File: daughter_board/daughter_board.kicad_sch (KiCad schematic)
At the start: 30 parts, among them J1 Conn_01x05_Female, J3 Conn_01x06_Male, J4 Conn_01x06_Male, J5 Conn_01x02_Male, J6 Conn_01x02_Male, J7 Conn_01x06_Male, J8 Conn_01x06_Male, U1 ATmega32U4-A, U2 DRV8833PW, U3 DRV8833PW, U4 DRV8833PW, Y1 Crystal

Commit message: im so tired
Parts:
- removed C10: 0.1uF, Capacitor_SMD:C_0805_2012Metric, symbol Device:C_Small
- removed C12: 2.2uF, Capacitor_SMD:C_0805_2012Metric, symbol Device:C_Small
- removed C13: 10uF, Capacitor_SMD:C_0805_2012Metric, symbol Device:C_Small
- removed J5, J6: Conn_01x02_Male, Connector_PinHeader_1.27mm:PinHeader_1x02_P1.27mm_Vertical, symbol Connector:Conn_01x02_Male
- removed U3: DRV8833PW, Package_SO:TSSOP-16_4.4x5mm_P0.65mm, symbol Driver_Motor:DRV8833PW
- added SW1: SW_Push, Button_Switch_SMD:SW_SPST_EVPBF, symbol Switch:SW_Push
- C1, C11, C14, C15, C2, C3, C4, C5, C6, C7, C8, C9: footprint Capacitor_SMD:C_0805_2012Metric -> Capacitor_SMD:C_0402_1005Metric
- Y1: footprint Crystal:Crystal_SMD_SeikoEpson_FA238-4Pin_3.2x2.5mm -> Crystal:TXC_A308000003
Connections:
- net C_ENC_1: now also U1.29 (PB5); no longer U1.28 (PB4)
- net C_ENC_2: now also U1.28 (PB4); no longer U1.29 (PB5)
- net D_ENC_1: now also J8.6 (Pin_6); no longer J8.3 (Pin_3)
- net GND: now also SW1.2
- net MOTOR_A1_IN: now also U1.31 (PC6); no longer U1.32 (PC7)
- net MOTOR_A2_IN: now also U1.32 (PC7); no longer U1.31 (PC6)
- net MOTOR_B1_IN: now also U1.20 (PD2); no longer U1.21 (PD3)
- net MOTOR_B2_IN: now also U1.21 (PD3); no longer U1.20 (PD2)
- net MOTOR_SUPPLY: now also C15.1, C9.1, U2.12 (VM), U4.12 (VM)
- net RST: now reaches U1.13 (~{RESET})
- net RST: now also SW1.1
- net at U4.7 (BOUT1): now also J8.3 (Pin_3); no longer J8.6 (Pin_6)
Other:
- note removed: "MOTOR E-F"
- moved on the sheet: J8

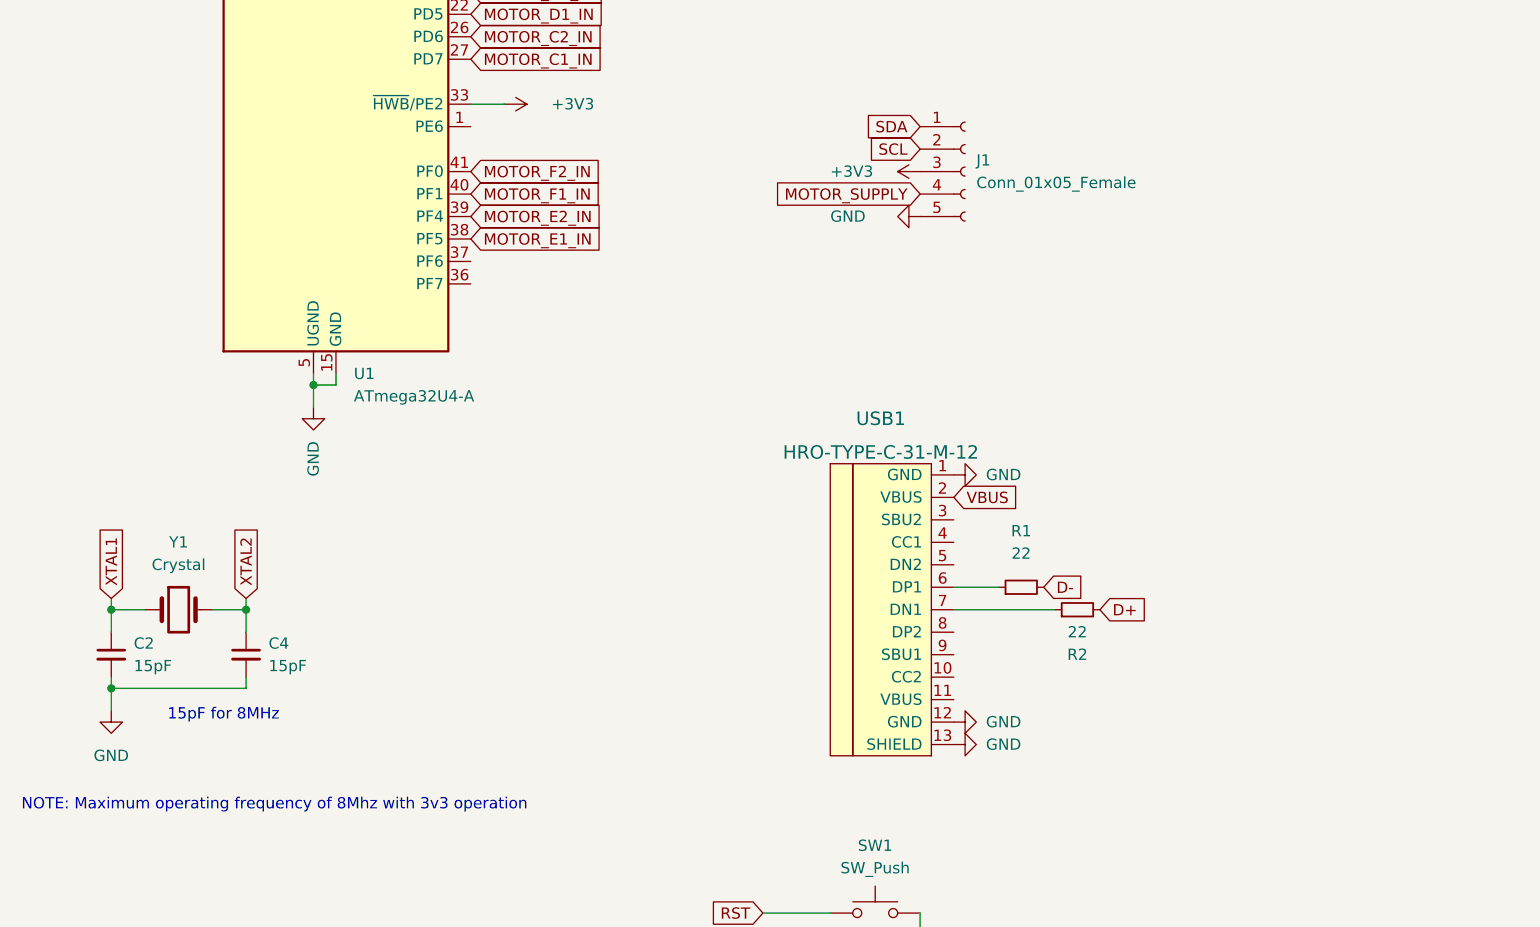
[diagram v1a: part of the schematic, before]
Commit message: Added daughter board
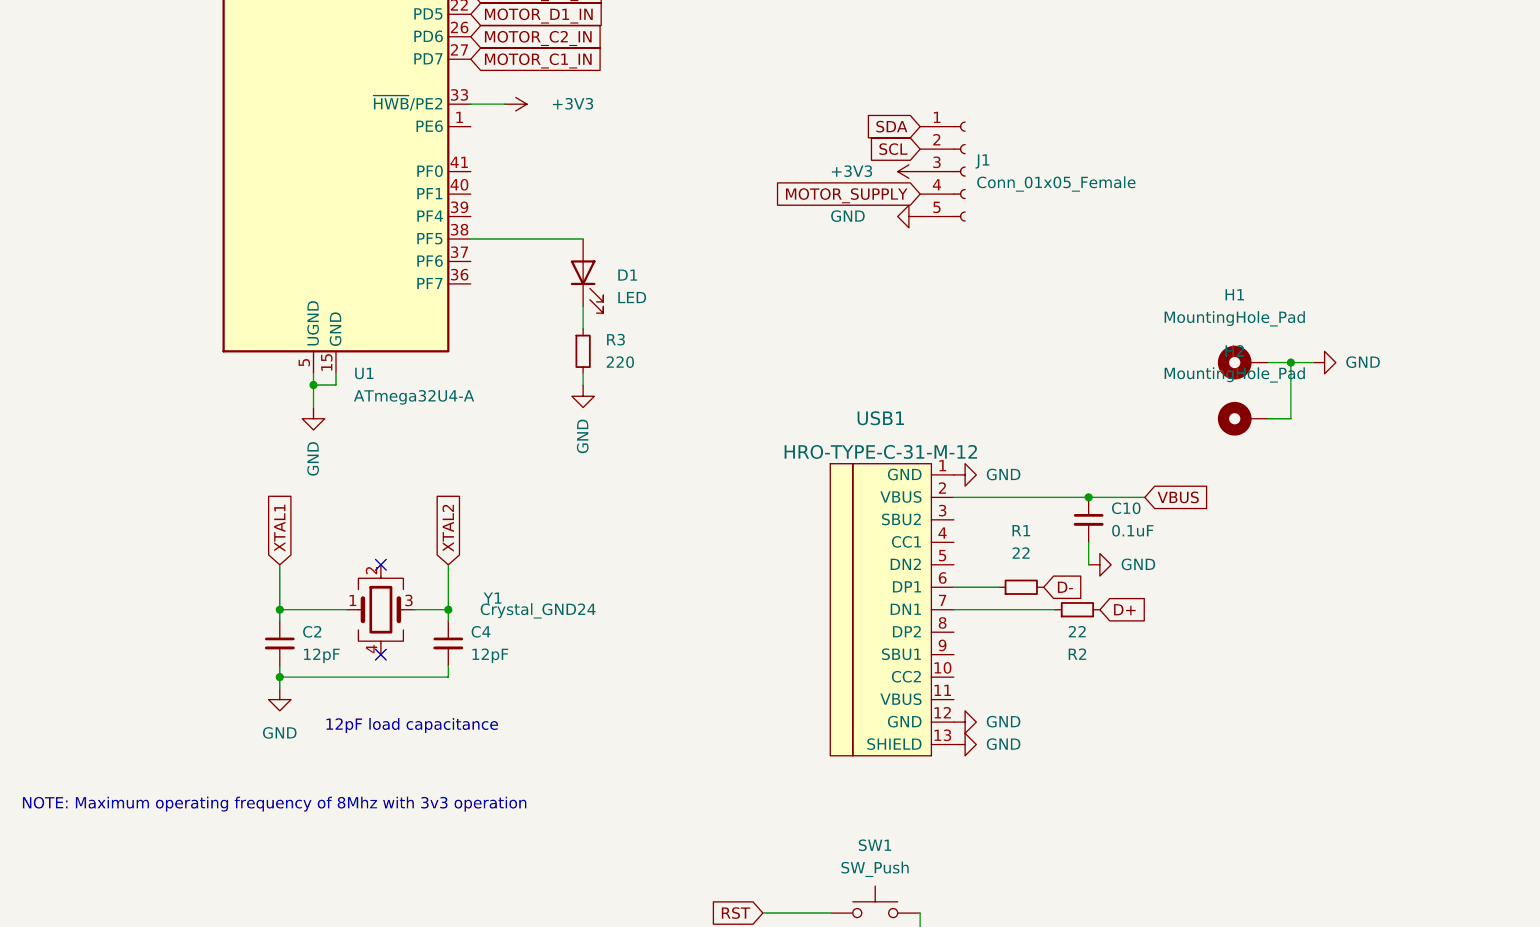
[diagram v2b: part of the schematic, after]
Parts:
- removed Y1: Crystal, Crystal:TXC_A308000003, symbol Device:Crystal
- added C10: 0.1uF, Capacitor_SMD:C_0402_1005Metric, symbol Device:C_Small
- added D1: LED, LED_SMD:LED_0402_1005Metric, symbol Device:LED
- added H1, H2: MountingHole_Pad, MountingHole:MountingHole_2.2mm_M2_DIN965_Pad, symbol Mechanical:MountingHole_Pad
- added R3: 220, Resistor_SMD:R_0402_1005Metric, symbol Device:R_Small
- added Y1: Crystal_GND24, Crystal:Crystal_SMD_3225-4Pin_3.2x2.5mm, symbol Device:Crystal_GND24
- C1, C3: LCSC (none) -> C106254
- C11, C5, C6, C7: LCSC (none) -> C141382
- C14, C8: LCSC (none) -> C76594
- C15, C9: LCSC (none) -> C87148
- C2, C4: value 15pF -> 12pF; LCSC (none) -> C106201
- R1, R2: LCSC (none) -> C881322
- U1: LCSC (none) -> C112161
- U2, U4: LCSC (none) -> C50506
- USB1: LCSC (none) -> C165948
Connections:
- net GND: now also C10.2, H1.1, H2.1, R3.2
- net VBUS: now also C10.1
- net XTAL1: now also Y1.1
- net XTAL2: now also Y1.3
- net MOTOR_E1_IN: no longer names the net of U1.38 (PF5)
- net MOTOR_E1_IN: now also D1.2 (A)
- net MOTOR_E2_IN: no longer names the net of U1.39 (PF4)
- net MOTOR_F1_IN: no longer names the net of U1.40 (PF1)
- net MOTOR_F2_IN: no longer names the net of U1.41 (PF0)
- new net: D1.1 (K), R3.1
- no-connect marks 1 -> 3
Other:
- note added: "12pF load capacitance"
- note removed: "15pF for 8MHz"
